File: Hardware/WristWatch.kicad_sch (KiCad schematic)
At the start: 53 parts, among them J1 vcc, J2 gnd, J3 vcc, J4 gnd, Q1 Q_PMOS_GSD, U1 BQ51051BRHL, U3 LIS2DE12, U4 AP2205-3.0, U5 MCP73832-2-OT, U6 ESP32-C3, Y2 40M, Y3 32.768k

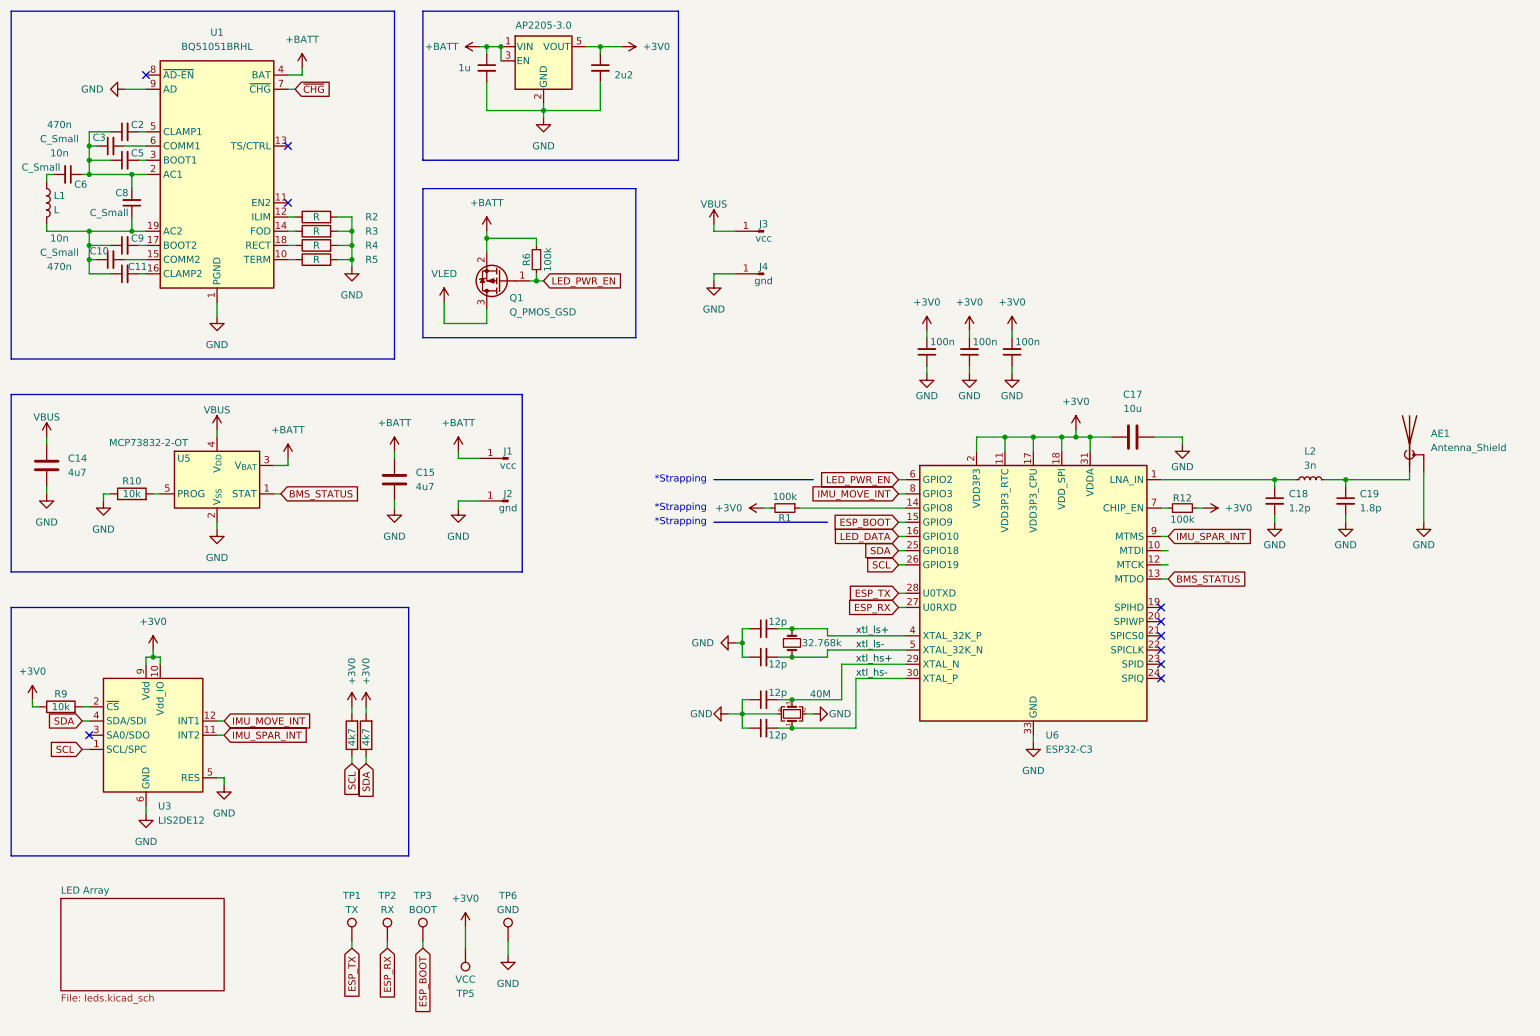
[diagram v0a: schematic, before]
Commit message: rev C for shift registered discrete 0603 LEDs
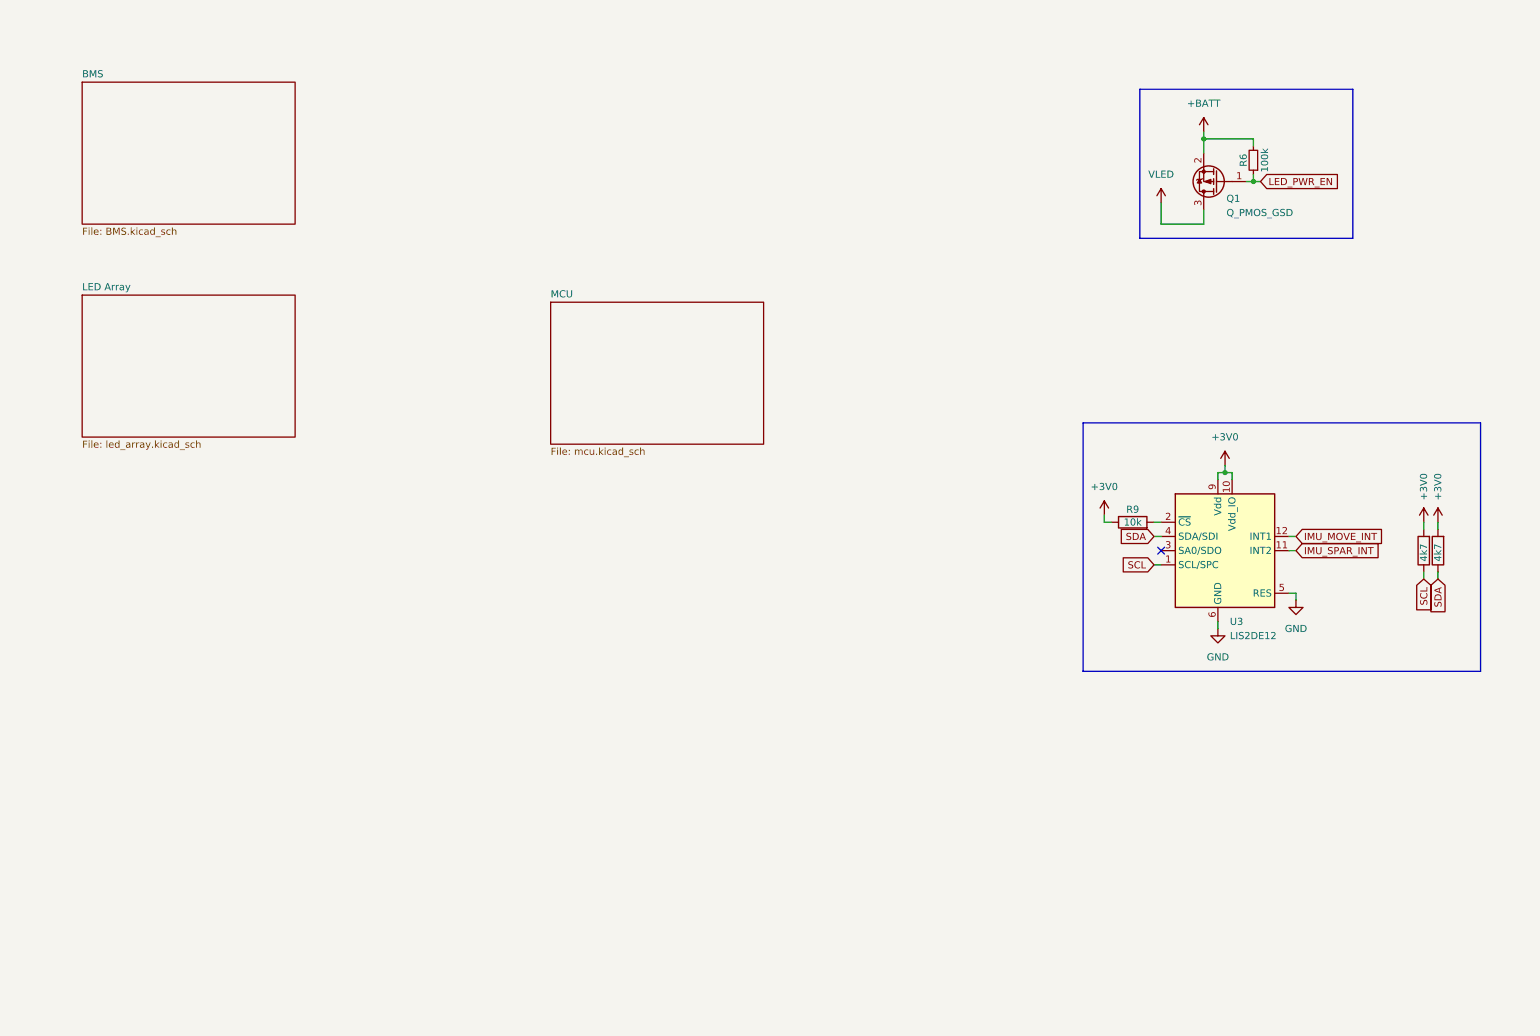
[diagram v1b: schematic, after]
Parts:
- removed AE1: Antenna_Shield, Antenna_SMD:C209892, symbol Device:Antenna_Shield
- removed C1, C16, C4, C7: 12p, symbol Device:C_Small
- removed C10, C3, C6, C8: C_Small, Capacitor_SMD:C_0402_1005Metric, symbol Device:C_Small
- removed C11, C2: 470n, Capacitor_SMD:C_0402_1005Metric, symbol Device:C_Small
- removed C12: 1u, Capacitor_SMD:C_0402_1005Metric, symbol Device:C_Small
- removed C13: 2u2, Capacitor_SMD:C_0402_1005Metric, symbol Device:C_Small
- removed C14, C15: 4u7, Capacitor_SMD:C_0402_1005Metric, symbol Device:C
- removed C17: 10u, symbol Device:C
- removed C18: 1.2p, Capacitor_SMD:C_0402_1005Metric, symbol Device:C_Small
- removed C19: 1.8p, Capacitor_SMD:C_0402_1005Metric, symbol Device:C_Small
- removed C20, C21, C22: 100n, Capacitor_SMD:C_0402_1005Metric, symbol Device:C_Small
- removed C5, C9: 10n, Capacitor_SMD:C_0402_1005Metric, symbol Device:C_Small
- removed J1, J3: vcc, TestPoint:TestPoint_Pad_D1.0mm, symbol Connector:Conn_01x01_Pin
- removed J2, J4: gnd, TestPoint:TestPoint_Pad_D1.0mm, symbol Connector:Conn_01x01_Pin
- removed L1: L, Connector_PinHeader_1.27mm:PinHeader_1x02_P1.27mm_Vertical, symbol Device:L
- removed L2: 3n, Inductor_SMD:L_0402_1005Metric, symbol Device:L_Small
- removed R1, R12: 100k, Resistor_SMD:R_0402_1005Metric, symbol Device:R_Small
- removed R10: 10k, Resistor_SMD:R_0402_1005Metric, symbol Device:R
- removed R2, R3, R4, R5: R, Resistor_SMD:R_0402_1005Metric, symbol Device:R
- removed TP1: TX, TestPoint:TestPoint_Pad_D1.5mm, symbol Connector:TestPoint
- removed TP2: RX, TestPoint:TestPoint_Pad_D1.5mm, symbol Connector:TestPoint
- removed TP3: BOOT, TestPoint:TestPoint_Pad_D1.5mm, symbol Connector:TestPoint
- removed TP5: VCC, TestPoint:TestPoint_Pad_D1.5mm, symbol Connector:TestPoint
- removed TP6: GND, TestPoint:TestPoint_Pad_D1.5mm, symbol Connector:TestPoint
- removed U1: BQ51051BRHL, Package_DFN_QFN:Texas_VQFN-RHL-20, symbol Battery_Management:BQ51051BRHL
- removed U4: AP2205-3.0, Package_TO_SOT_SMD:SOT-23-5, symbol Regulator_Linear:AP2127K-3.0
- removed U5: MCP73832-2-OT, Package_TO_SOT_SMD:SOT-23-5, symbol Battery_Management:MCP73832-2-OT
- removed U6: ESP32-C3, Package_DFN_QFN:QFN-32-1EP_5x5mm_P0.5mm_EP3.7x3.7mm, symbol MCU_Espressif:ESP32-C3
- removed Y2: 40M, Crystal:Crystal_SMD_2520-4Pin_2.5x2.0mm, symbol Device:Crystal_GND24_Small
- removed Y3: 32.768k, Crystal:Crystal_SMD_EuroQuartz_EQ161-2Pin_3.2x1.5mm, symbol Device:Crystal_Small
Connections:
- no-connect marks 10 -> 1
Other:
- added sheet BMS (BMS.kicad_sch)
- added sheet MCU (mcu.kicad_sch)
- sheet LED Array: file leds.kicad_sch -> led_array.kicad_sch
- note removed: "*Strapping"
- moved on the sheet: Q1, R6, R9, U3

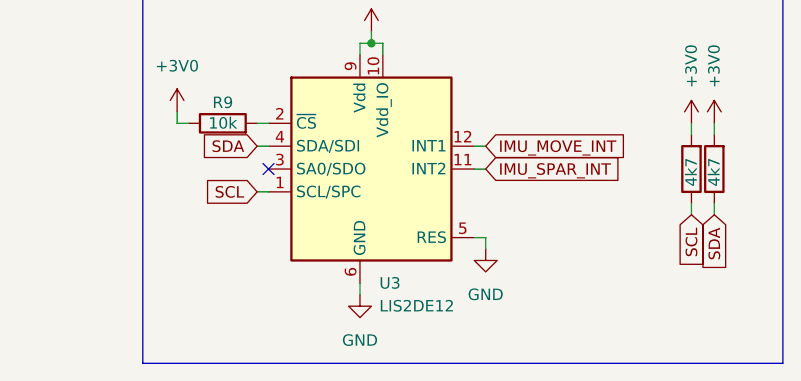
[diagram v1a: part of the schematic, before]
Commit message: semi-final component placements and final component selections. Abandoning due to high routing complexity and need for a 4L board.
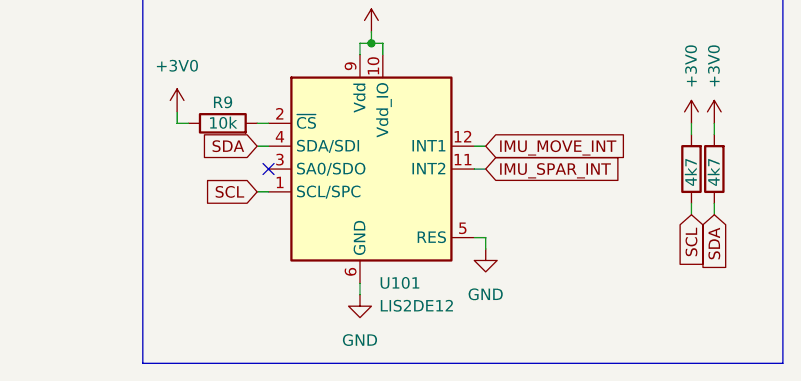
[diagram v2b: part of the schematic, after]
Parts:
- renumbered U3 to U101
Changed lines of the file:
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@@
 		(dnp no)
 		(fields_autoplaced yes)
-		(property "Reference" "U3"
+		(property "Reference" "U101"
 			(at 230.7433 121.92 0)
 			(effects
@@
 			(project ""
 				(path "/fa78ac01-f44d-4d2a-889a-213ee2d7711c"
-					(reference "U3")
+					(reference "U101")
 					(unit 1)
 				)
